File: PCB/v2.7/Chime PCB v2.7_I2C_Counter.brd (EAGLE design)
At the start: 64.8 x 78.8 mm, 31 parts, among them J1_SPI 1725698, J2_I2C 1725672, J4_A1 282834-3, J5_A0 282834-3, U1 MS5803-02BA, X4 BQ24074

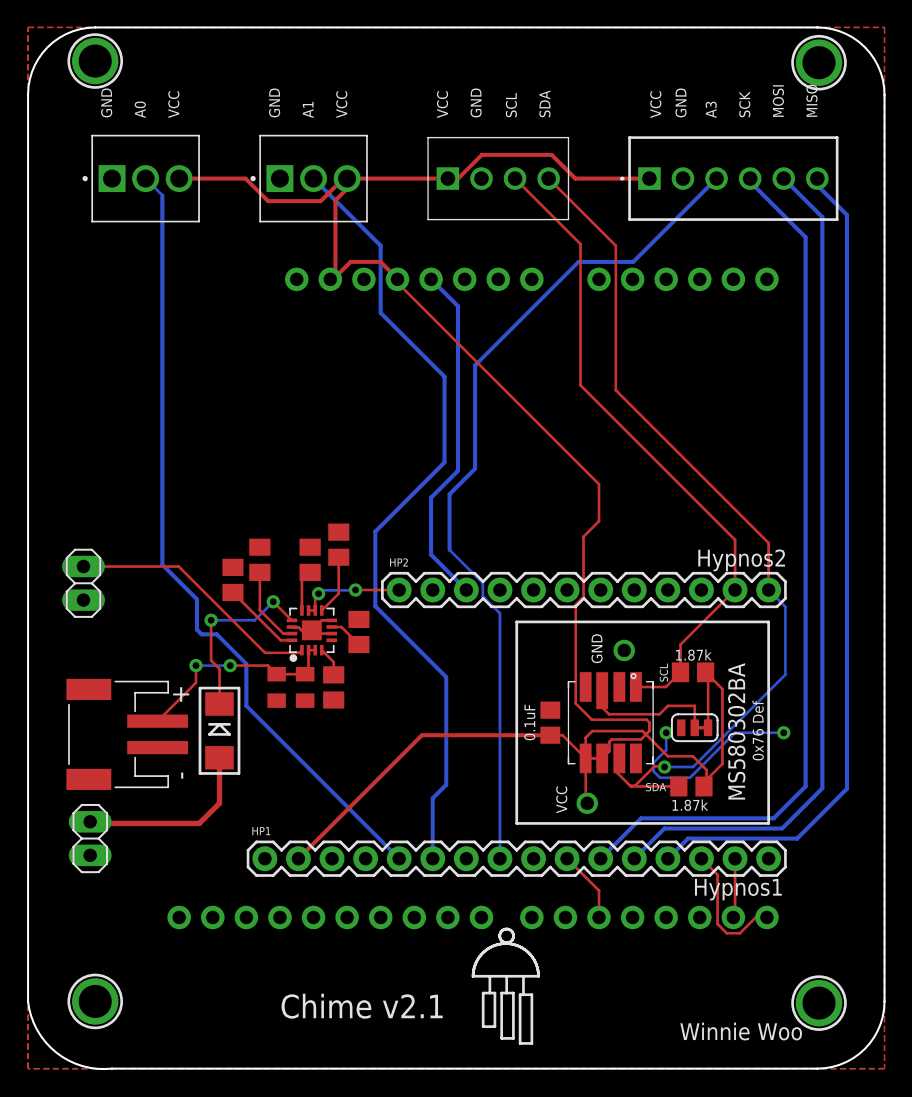
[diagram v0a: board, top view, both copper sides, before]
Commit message: Adding final I2C_Extender and Chime PCB board file
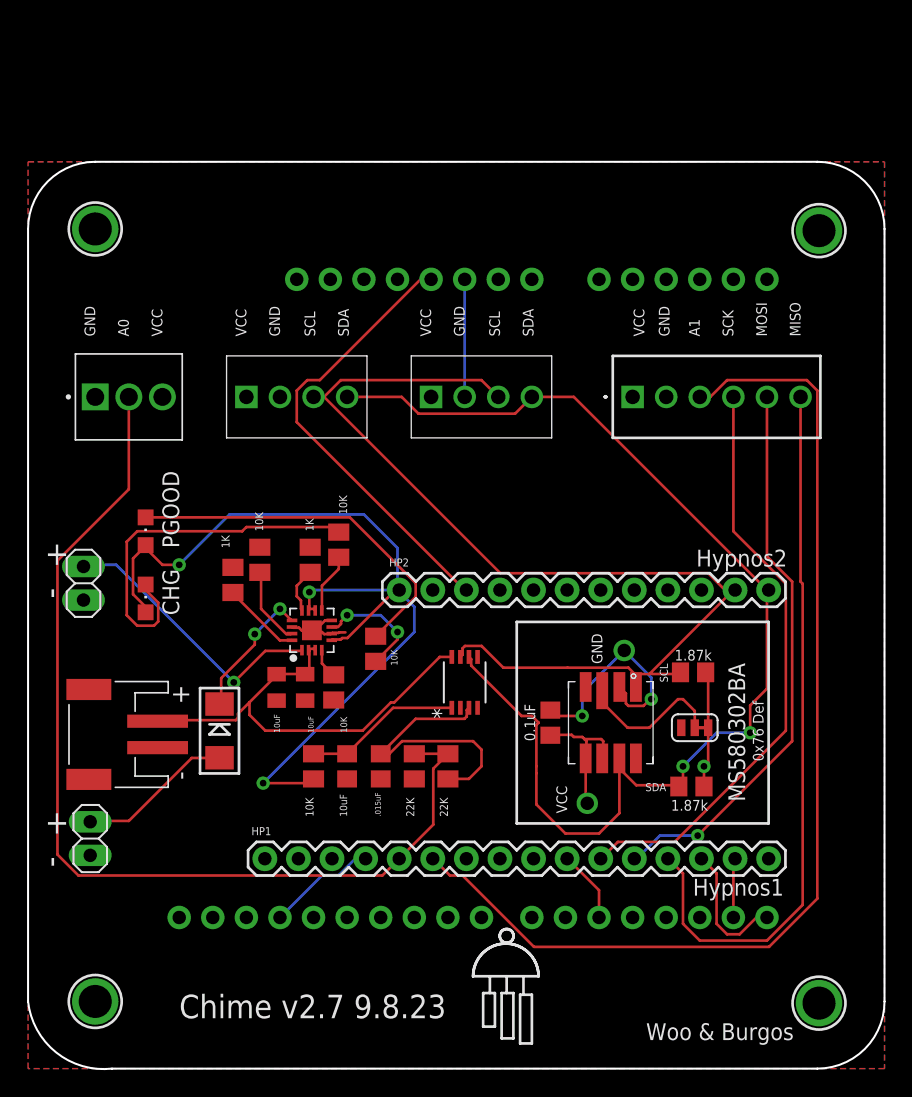
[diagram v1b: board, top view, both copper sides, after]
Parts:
- removed J4_A1: 282834-3, Fixed Terminal Blocks 3P:TE_282834-3
- added C2: 10uF, rcl:C0805
- added C3: 15nF, rcl:C0805
- added CHG: (no value), adafruit:CHIPLED_0805
- added J2_I2C1: 1725672, 1725672:1725672
- added PGOOD: PGOOD, adafruit:CHIPLED_0805
- added R10: 10K, adafruit:M0805
- added R5, R6: 22K, adafruit:M0805
- added U2: S-35770E01I-K8T2U, S-35770 COUNTER:TMSOP08_2P9X2P8_ABL
- moved J1_SPI 16.6 mm to (44.5, 49.5)
- moved J2_I2C 16.6 mm to (29.2, 49.5)
- moved J5_A0 16.6 mm to (3.81, 49.5)
- moved U$3 12.7 mm to (3.81, 62.2)
- moved U$4 12.7 mm to (58.5, 62.1)
- moved R11 1.80 mm to (25.0, 30.5)
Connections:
- removed net N$1: X4.5
- new net CLKIN: C3.1, R5.1, U2.3
- new net N$4: PGOOD.C, R11.2
- new net N$5: CHG.C, R7.2
- new net REST: C2.1, R10.2, U2.1
- net A0: now also R5.2, R6.1
- net A1: now also J1_SPI.3; no longer J4_A1.2
- net A3: no longer J1_SPI.3
- net GND: now also C2.2, C3.2, J2_I2C1.2, JP9.2, R6.2, U2.4; no longer J4_A1.1
- net SCL: now also J2_I2C1.3, U2.7
- net SDA: now also J2_I2C1.4, U2.6
- net VBAT: now also CHG.A, PGOOD.A, R10.1, X4.5
- net VCC: now also J2_I2C1.1; no longer J4_A1.3
- net VLIPO: now also U2.8
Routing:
- net VCC: track 161.6 -> 19.4 mm, vias 0 -> 1
- net A3: track 63.8 -> 0.00 mm
- net VBAT: track 8.09 -> 70.6 mm, vias 2 -> 3
- net SCL: track 49.8 -> 81.7 mm
- net N$5: track 0.00 -> 28.3 mm
- net N$4: track 0.00 -> 27.8 mm
- net SDA: track 66.4 -> 89.0 mm, vias 1 -> 2
- net MOSI: track 63.7 -> 42.4 mm, vias 0 -> 1
- net A1: track 60.3 -> 81.5 mm
- net CLKIN: track 0.00 -> 20.9 mm
- net SCK: track 65.5 -> 44.9 mm
- net GND: track 19.8 -> 40.3 mm
- net VLIPO: track 16.4 -> 34.5 mm, vias 2 -> 0
- net A0: track 60.1 -> 75.9 mm
- net REST: track 0.00 -> 11.9 mm
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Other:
- board size 64.8 x 78.8 mm -> 64.8 x 68.6 mm
- board text added: "+"
- board text added: "-"
- board text added: ".015uF"
- board text added: "10K"
- board text added: "10uF"
- board text added: "1K"
- board text added: "22K"
- board text added: "Chime v2.7 9.8.23"
- board text added: "Woo & Burgos"
- board text removed: "A3"
- board text removed: "Chime v2.1"
- board text removed: "Winnie Woo"
